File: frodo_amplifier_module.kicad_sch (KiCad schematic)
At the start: 43 parts, among them IC1 INA826AID, J1 JST-GH, J2 JST-GH, J3 Conn_01x02_Socket, J5 Conn_01x04_Socket, U2 MCP6001-OT, U3 MIC5504-3.3YM5, U4 ADC101C021CIMM

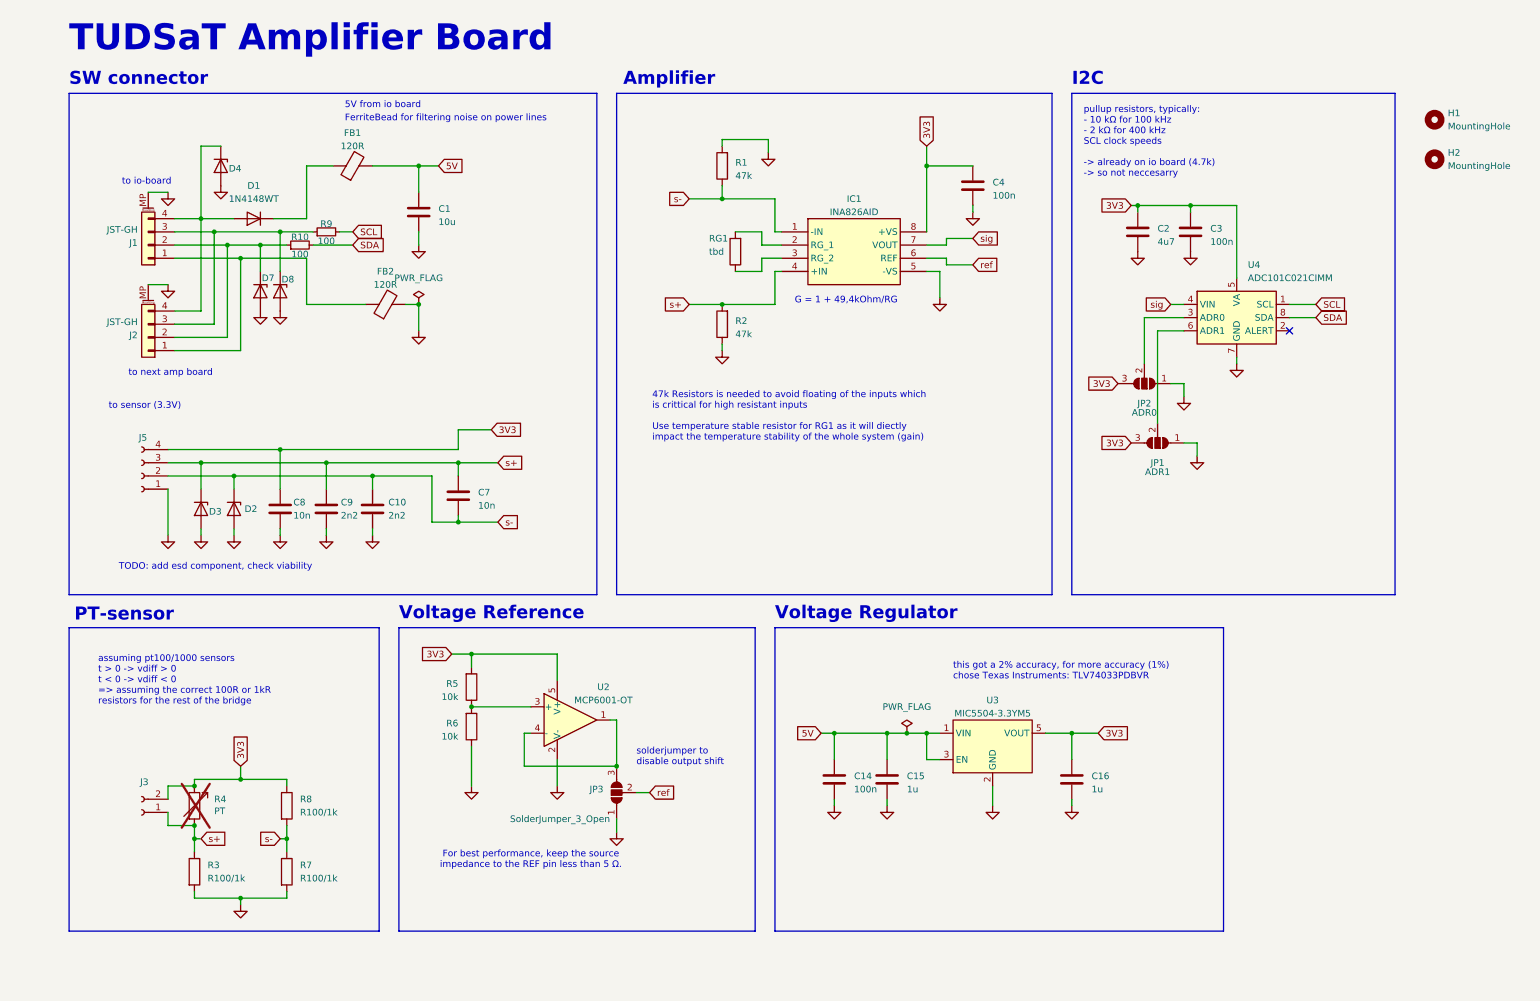
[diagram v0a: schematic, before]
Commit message: added lcsc numbers
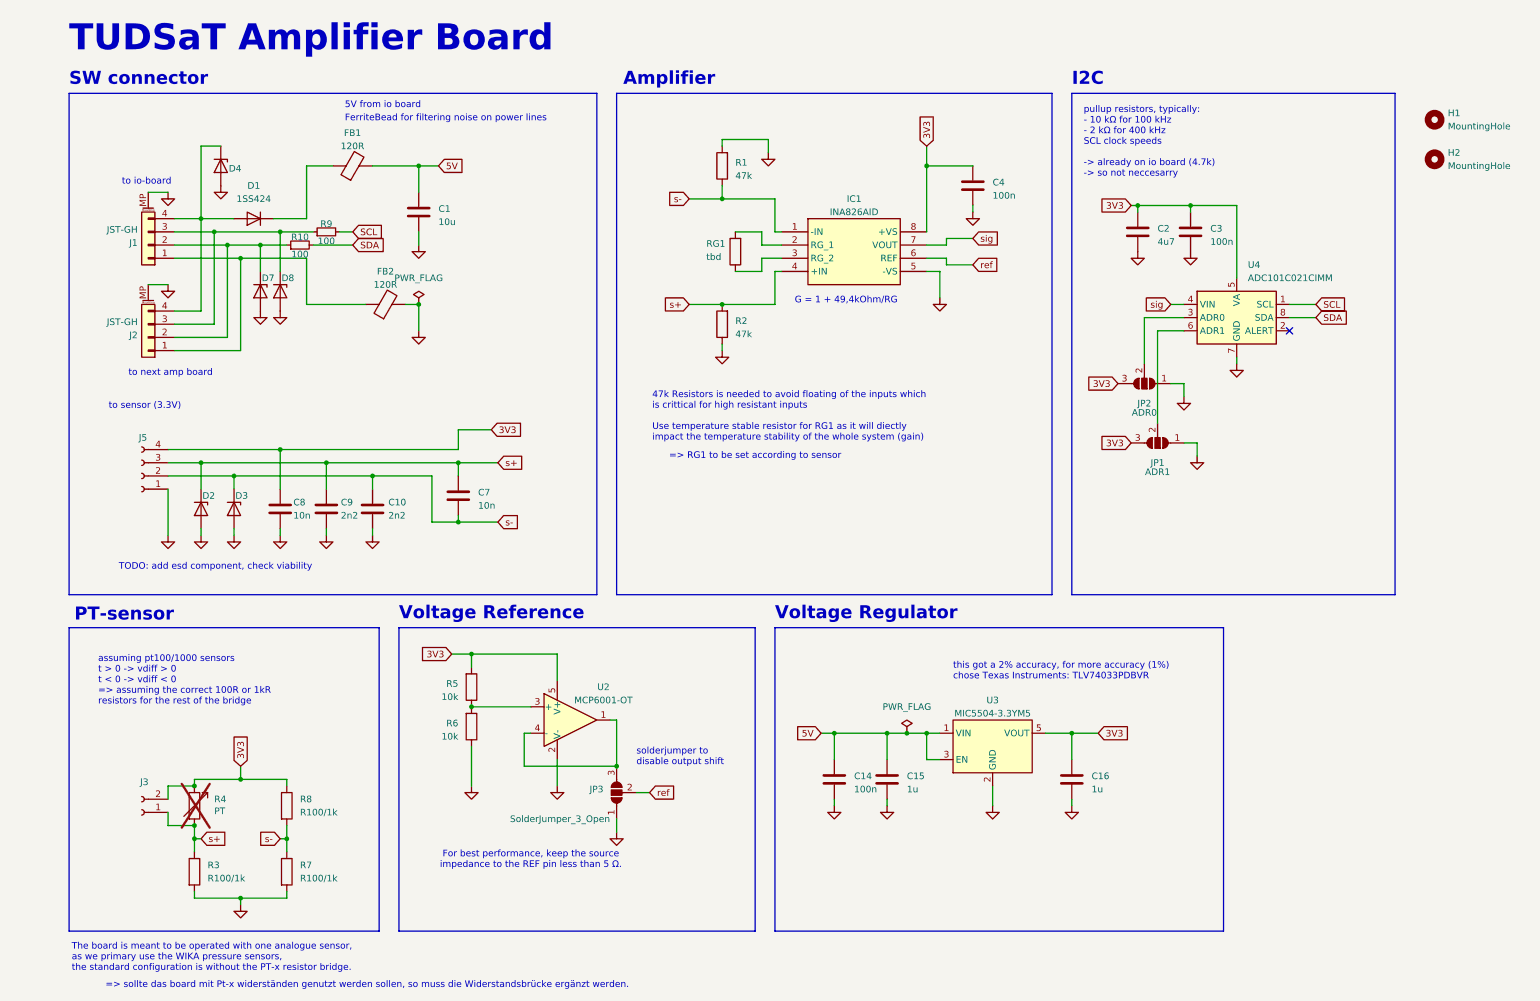
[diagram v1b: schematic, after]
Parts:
- D1: value 1N4148WT -> 1SS424; LCSC (none) -> C6657698
- D2, D3, D7, D8: value ESD5Zxx -> ESD5Z36; LCSC (none) -> C48935658
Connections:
- net s+: now also D2.1 (K); no longer D3.1 (K)
- net s-: now also D3.1 (K); no longer D2.1 (K)
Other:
- note added: "=> RG1 to be set according to sensor"
- note added: "=> sollte das board mit Pt-x widerständen genutzt werden sollen, so muss die Widerstandsbrücke ergänzt werden."
- note added: "The board is meant to be operated with one analogue sensor, as we primary use the WIKA pressure sensors, the standard configuration is without the PT-x resistor bridge."
